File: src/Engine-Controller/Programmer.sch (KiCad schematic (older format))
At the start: 1 part, among them J3 SBH11-PBPC-D05-RA-BK

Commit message: Associated Schematic Symbols with footprints
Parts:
- J3: footprint 66953-005LF_AMP -> Engine-Controller:SBH11-PBPC-D05-RA-BK
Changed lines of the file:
@@
 F 0 "J3" H 5692 3887 60  0000 C CNN
 F 1 "SBH11-PBPC-D05-RA-BK" H 5692 3781 60  0000 C CNN
-F 2 "66953-005LF_AMP" H 5600 2400 60  0001 C CNN
+F 2 "Engine-Controller:SBH11-PBPC-D05-RA-BK" H 5600 2400 60  0001 C CNN
 F 3 "" H 5450 3600 60  0000 C CNN
 	1    5450 3600

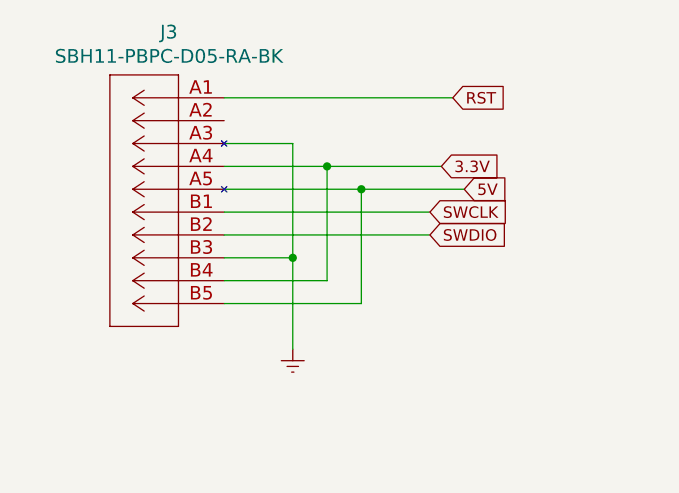
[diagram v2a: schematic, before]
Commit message: Updated Connector pinouts and added button to Reset pin
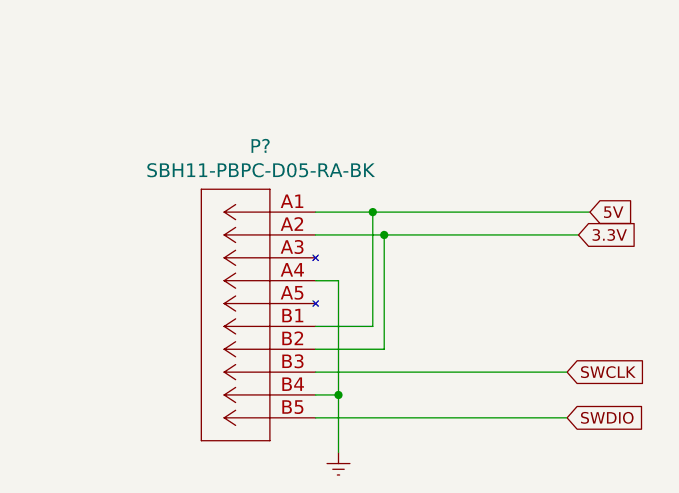
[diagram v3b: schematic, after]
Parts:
- removed J3: SBH11-PBPC-D05-RA-BK, Engine-Controller:SBH11-PBPC-D05-RA-BK, symbol Engine-Controller:SBH11-PBPC-D05-RA-BK
- added P?: SBH11-PBPC-D05-RA-BK, 66953-005LF_AMP, symbol Engine-Controller:SBH11-PBPC-D05-RA-BK
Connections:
- net 3.3V: now also P?.A2, P?.B2
- net 5V: now also P?.A1, P?.B1
- net Earth: now also P?.A4, P?.B4
- net SWCLK: now also P?.B3
- net SWDIO: now also P?.B5
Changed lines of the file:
@@
 Comment4 ""
 $EndDescr
-Text GLabel 6450 3600 2    50   Input ~ 0
-RST
-Text GLabel 6350 4100 2    50   Input ~ 0
+Text GLabel 6950 4800 2    50   Input ~ 0
 SWCLK
-Text GLabel 6350 4200 2    50   Input ~ 0
+Text GLabel 6950 5000 2    50   Input ~ 0
 SWDIO
-Text GLabel 6400 3900 2    50   Input ~ 0
+Text GLabel 7000 4200 2    50   Input ~ 0
 3.3V
-Text GLabel 6500 4000 2    50   Input ~ 0
+Text GLabel 7050 4100 2    50   Input ~ 0
 5V
-Wire Wire Line
-	5450 3600 6450 3600
 $Comp
 L power:Earth #PWR0111
 U 1 1 60FCD9C3
-P 5750 4700
-F 0 "#PWR0111" H 5750 4450 50  0001 C CNN
-F 1 "Earth" H 5750 4550 50  0001 C CNN
-F 2 "" H 5750 4700 50  0001 C CNN
-F 3 "~" H 5750 4700 50  0001 C CNN
-	1    5750 4700
+P 5950 5150
+F 0 "#PWR0111" H 5950 4900 50  0001 C CNN
+F 1 "Earth" H 5950 5000 50  0001 C CNN
+F 2 "" H 5950 5150 50  0001 C CNN
+F 3 "~" H 5950 5150 50  0001 C CNN
+	1    5950 5150
 	1    0    0    -1
 $EndComp
-Wire Wire Line
-	5450 3800 5750 3800
-Wire Wire Line
-	5750 3800 5750 4300
-Wire Wire Line
-	6400 3900 5900 3900
-Wire Wire Line
-	6500 4000 6050 4000
-Wire Wire Line
-	6350 4100 5450 4100
-Wire Wire Line
-	6350 4200 5450 4200
-Wire Wire Line
-	5450 4300 5750 4300
-Connection ~ 5750 4300
-Wire Wire Line
-	5750 4300 5750 4700
-Wire Wire Line
-	5450 4400 5900 4400
-Wire Wire Line
-	5900 4400 5900 3900
-Connection ~ 5900 3900
-Wire Wire Line
-	5900 3900 5450 3900
-Wire Wire Line
-	5450 4500 6050 4500
-Wire Wire Line
-	6050 4500 6050 4000
-Connection ~ 6050 4000
-Wire Wire Line
-	6050 4000 5450 4000
 $Comp
-L Engine-Controller:SBH11-PBPC-D05-RA-BK J3
-U 1 1 6128428C
-P 5450 3600
-F 0 "J3" H 5692 3887 60  0000 C CNN
-F 1 "SBH11-PBPC-D05-RA-BK" H 5692 3781 60  0000 C CNN
-F 2 "Engine-Controller:SBH11-PBPC-D05-RA-BK" H 5600 2400 60  0001 C CNN
-F 3 "" H 5450 3600 60  0000 C CNN
-	1    5450 3600
+L Engine-Controller:SBH11-PBPC-D05-RA-BK P?
+U 1 1 60E49761
+P 5850 4100
+F 0 "P?" H 6092 4387 60  0000 C CNN
+F 1 "SBH11-PBPC-D05-RA-BK" H 6092 4281 60  0000 C CNN
+F 2 "66953-005LF_AMP" H 6000 2900 60  0001 C CNN
+F 3 "" H 5850 4100 60  0001 C CNN
+	1    5850 4100
 	-1   0    0    -1
 $EndComp
+Wire Wire Line
+	5850 4100 6100 4100
+Wire Wire Line
+	5850 4600 6100 4600
+Wire Wire Line
+	6100 4600 6100 4100
+Connection ~ 6100 4100
+Wire Wire Line
+	6100 4100 7050 4100
+Wire Wire Line
+	5850 4400 5950 4400
+Wire Wire Line
+	5950 4400 5950 4900
+Wire Wire Line
+	5850 4900 5950 4900
+Connection ~ 5950 4900
+Wire Wire Line
+	5950 4900 5950 5150
+Wire Wire Line
+	7000 4200 6150 4200
+Wire Wire Line
+	5850 4700 6150 4700
+Wire Wire Line
+	6150 4700 6150 4200
+Connection ~ 6150 4200
+Wire Wire Line
+	6150 4200 5850 4200
+Wire Wire Line
+	6950 5000 5850 5000
+Wire Wire Line
+	5850 4800 6950 4800
 $EndSCHEMATC

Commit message: Added buffer to some IOs
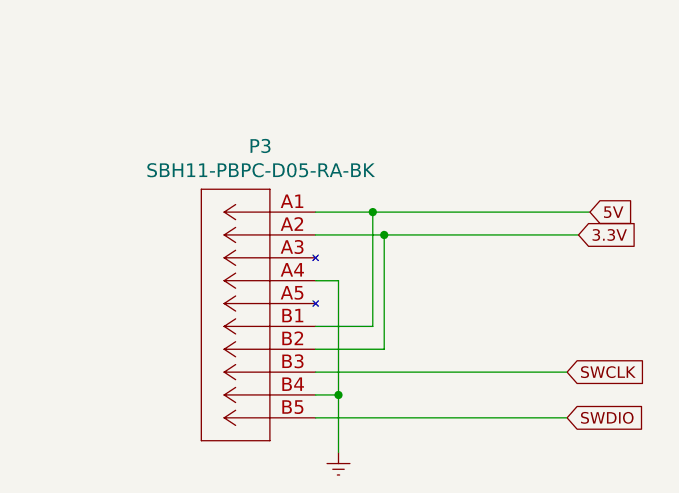
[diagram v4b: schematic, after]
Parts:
- gave numbers to parts that had none: 1
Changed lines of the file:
@@
 $EndComp
 $Comp
-L Engine-Controller:SBH11-PBPC-D05-RA-BK P?
+L Engine-Controller:SBH11-PBPC-D05-RA-BK P3
 U 1 1 60E49761
 P 5850 4100
-F 0 "P?" H 6092 4387 60  0000 C CNN
+F 0 "P3" H 6092 4387 60  0000 C CNN
 F 1 "SBH11-PBPC-D05-RA-BK" H 6092 4281 60  0000 C CNN
 F 2 "66953-005LF_AMP" H 6000 2900 60  0001 C CNN
